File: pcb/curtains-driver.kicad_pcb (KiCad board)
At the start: 2 copper layers, 71 x 29.7 mm, 25 parts, among them J1 Barrel_Jack, J2 UART, J3 Motor, SW1 Reed_NC, SW2 Reed_NC, SW3 UP, SW4 DOWN, SW5 FLASH, U1 ESP-12F, U2 LM1117-3.3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

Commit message: Refactor Circuit
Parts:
- removed R9: 10K, Resistor_SMD:R_0805_2012Metric_Pad1.15x1.40mm_HandSolder
- added C5: 0.1uF, Capacitor_SMD:C_1206_3216Metric_Pad1.42x1.75mm_HandSolder, B.Cu at (115.8, 90.2)
- added SW6: RESET, Button_Switch_SMD:SW_SPST_CK_RS282G05A3, F.Cu at (110.7, 76.3)
- R1, R2, R3, R4: value 10K -> R; moved to B.Cu
- R5, R6, R7: value 10K -> R
- R8: value 5K1 -> 56K
- SW5: footprint Connector_PinHeader_2.54mm:PinHeader_1x02_P2.54mm_Vertical -> Button_Switch_SMD:SW_SPST_CK_RS282G05A3
- moved J1 44.7 mm to (90.7, 83.3), turned to 90 degrees
- moved C4 35.3 mm to (91.5, 76.2), turned to 180 degrees
- moved C2 30.7 mm to (98.8, 74.9), turned to 0 degrees
- moved U2 30.1 mm to (94.1, 69.0)
- moved J2 26.4 mm to (80.8, 65.5), turned to 90 degrees
- moved SW4 19.7 mm to (128.1, 70.2), turned to 90 degrees
- moved SW1 17.3 mm to (128.1, 83.0), turned to 90 degrees
- moved SW3 14.2 mm to (128.1, 76.0), turned to 90 degrees
- moved R4 13.2 mm to (118.5, 85.4), turned to 270 degrees
- moved SW5 12.8 mm to (105.4, 76.3), turned to 270 degrees
- moved R1 10.6 mm to (119.5, 72.4), turned to 0 degrees
- moved SW2 9.40 mm to (128.1, 88.8), turned to 90 degrees
- moved R2 8.70 mm to (119.5, 76.4), turned to 0 degrees
- moved R7 6.52 mm to (96.8, 80.4), turned to 0 degrees
- moved R8 5.86 mm to (119.5, 70.4), turned to 0 degrees
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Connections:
- C4 pad 1: +3V3 -> VCC
- J2 pad 4: +3V3 -> VCC
- R1 pad 1: +3V3 -> Net-(R1-Pad1)
- R1 pad 2: Net-(C1-Pad1) -> VCC
- R2 pad 1: +3V3 -> Net-(R2-Pad1)
- R2 pad 2: Net-(C3-Pad1) -> VCC
- R3 pad 1: +3V3 -> Net-(C1-Pad1)
- R3 pad 2: Net-(R3-Pad2) -> VCC
- R4 pad 1: +3V3 -> Net-(C3-Pad1)
- R4 pad 2: Net-(R4-Pad2) -> VCC
- R5 pad 1: +3V3 -> Earth
- R6 pad 1: +3V3 -> VCC
- R7 pad 1: Earth -> VCC
- SW3 pad 1: +3V3 -> VCC
- SW3 pad 2: Net-(R8-Pad2) -> ADC
- SW4 pad 1: +3V3 -> VCC
- SW4 pad 2: Net-(R9-Pad2) -> Net-(R8-Pad2)
- SW5 pad 1: Earth -> Net-(R7-Pad2)
- SW5 pad 2: Net-(R5-Pad2) -> Earth
- U1 pad 1: Net-(R4-Pad2) -> Net-(R1-Pad1)
- U1 pad 10: Net-(R7-Pad2) -> Net-(R5-Pad2)
- U1 pad 12: Net-(R5-Pad2) -> Net-(R7-Pad2)
- U1 pad 3: Net-(R3-Pad2) -> Net-(R2-Pad1)
- U1 pad 8: +3V3 -> VCC
- U2 pad 2: +3V3 -> VCC
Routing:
- net VCC: track 0.00 -> 132.2 mm, vias 0 -> 2
- net +3V3: track 114.7 -> 0.00 mm
- net +5V: track 115.8 -> 30.8 mm, vias 0 -> 1
- net Net-(C1-Pad1): track 40.6 -> 13.8 mm, vias 1 -> 0
- net Net-(R9-Pad2): track 19.0 -> 0.00 mm, vias 1 -> 0
- net ADC: track 11.4 -> 29.6 mm
- net Net-(C3-Pad1): track 32.1 -> 15.7 mm, vias 1 -> 0
- net Net-(R7-Pad2): track 4.13 -> 15.2 mm, vias 0 -> 1
- net Net-(R5-Pad2): track 11.2 -> 3.26 mm
- net Net-(R1-Pad1): track 0.00 -> 7.76 mm, vias 0 -> 1
- net Net-(R8-Pad2): track 15.0 -> 8.65 mm, vias 1 -> 0
- net Net-(R6-Pad2): track 7.39 -> 3.26 mm
- net Net-(R3-Pad2): track 4.11 -> 0.00 mm, vias 1 -> 0
- net Net-(R4-Pad2): track 4.05 -> 0.00 mm, vias 1 -> 0
- net Net-(R2-Pad1): track 0.00 -> 3.42 mm
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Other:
- board size 71 x 29.7 mm -> 55 x 29.7 mm
- net class Resistor Array added: clearance 0.3, trace_width 0.6, via_dia 0.8, via_drill 0.4
- board text added: "brnv.ru"
- board text added: "curtains driver v1.1"

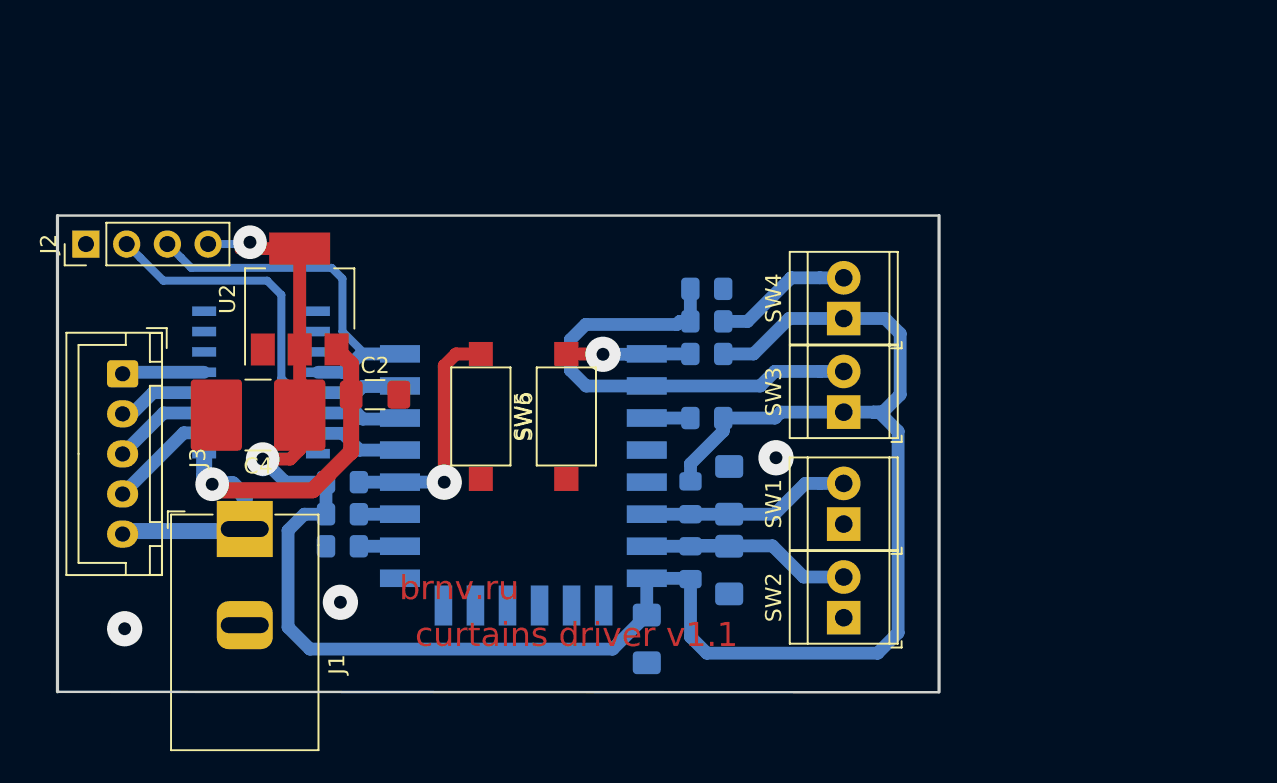
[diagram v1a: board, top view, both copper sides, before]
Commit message: Add USB-UART chip
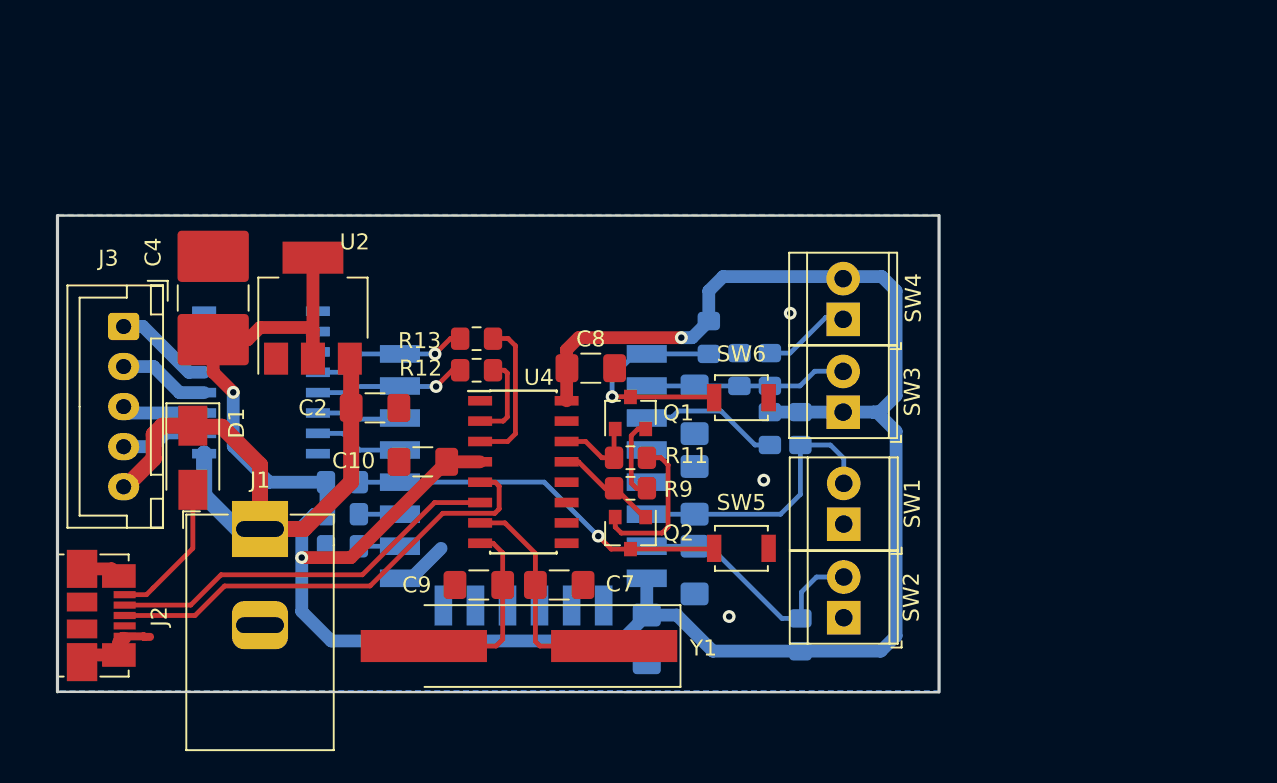
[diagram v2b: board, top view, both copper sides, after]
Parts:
- added C10: 10uF, Capacitor_SMD:C_1206_3216Metric_Pad1.42x1.75mm_HandSolder, F.Cu at (101.8, 79.1)
- added C6: 0.1uF, Capacitor_SMD:C_1206_3216Metric_Pad1.42x1.75mm_HandSolder, B.Cu at (118.7, 75.9)
- added C7: 22pF, Capacitor_SMD:C_1206_3216Metric_Pad1.42x1.75mm_HandSolder, F.Cu at (110.3, 86.8)
- added C8: 10uF, Capacitor_SMD:C_1206_3216Metric_Pad1.42x1.75mm_HandSolder, F.Cu at (112.3, 73.3)
- added C9: 22pF, Capacitor_SMD:C_1206_3216Metric_Pad1.42x1.75mm_HandSolder, F.Cu at (105.3, 86.8)
- added D1: M7, Diode_SMD:D_SMA, F.Cu at (87.4, 78.9)
- added Q1: S8050, Package_TO_SOT_SMD:SOT-23, F.Cu at (114.7, 76.1)
- added Q2: S8050, Package_TO_SOT_SMD:SOT-23, F.Cu at (114.7, 83.6)
- added R11: 10K, Resistor_SMD:R_0805_2012Metric_Pad1.15x1.40mm_HandSolder, F.Cu at (114.7, 78.9)
- added R12: 470, Resistor_SMD:R_0805_2012Metric_Pad1.15x1.40mm_HandSolder, F.Cu at (105.1, 73.4)
- added R13: 470, Resistor_SMD:R_0805_2012Metric_Pad1.15x1.40mm_HandSolder, F.Cu at (105.1, 71.4)
- added R9: 10K, Resistor_SMD:R_0805_2012Metric_Pad1.15x1.40mm_HandSolder, F.Cu at (114.7, 80.8)
- added U4: CH340G, Package_SO:SOIC-16_3.9x9.9mm_P1.27mm, F.Cu at (108.1, 79.8)
- added Y1: HC-49, Crystal:Crystal_SMD_HC49-SD_HandSoldering, F.Cu at (107.8, 90.6)
- J2: value UART -> USB_B_Micro; footprint Connector_PinHeader_2.54mm:PinHeader_1x04_P2.54mm_Vertical -> Connector_USB:USB_Micro-B_Molex_47346-0001
- R1, R2, R3, R4, R5, R6, R7: value R -> 10K
- SW5, SW6: footprint Button_Switch_SMD:SW_SPST_CK_RS282G05A3 -> Button_Switch_SMD:SW_SPST_B3U-1000P
- moved J2 23.2 mm to (81.7, 88.7), turned to 270 degrees
- moved SW5 18.2 mm to (121.7, 84.5), turned to 0 degrees
- moved SW6 11.0 mm to (121.7, 75.1), turned to 180 degrees
- moved R4 8.20 mm to (125.3, 89.9)
- moved R3 8.10 mm to (125.3, 77.0)
- moved C4 7.82 mm to (88.7, 68.9), turned to 90 degrees
- moved R10 5.43 mm to (121.5, 73.4), turned to 270 degrees
- moved R8 4.95 mm to (123.4, 73.4), turned to 90 degrees
- moved R2 3.99 mm to (123.4, 77.0), turned to 90 degrees
- moved J3 2.95 mm to (83.1, 70.7)
- moved C1 2.16 mm to (118.7, 80.9)
- moved C3 2.16 mm to (118.7, 85.9)
- moved R1 1.04 mm to (119.6, 71.4), turned to 90 degrees
- moved U2 1.00 mm to (94.9, 69.5)
- moved J1 0.95 mm to (91.6, 83.3)
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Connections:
- net Net-(R1-Pad1) renamed RST
- net Net-(R7-Pad2) renamed GPIO0
- J2 pad 1: Earth -> Net-(D1-Pad2)
- J2 pad 4: VCC -> Net-(J2-Pad4)
- SW4 pad 1: VCC -> Net-(R8-Pad2)
- SW4 pad 2: Net-(R8-Pad2) -> VCC
- U1 pad 15: Net-(J2-Pad2) -> RXD
- U1 pad 16: Net-(J2-Pad3) -> TXD
- U3 pad 4: Net-(J2-Pad3) -> TXD
- U3 pad 5: Net-(J2-Pad2) -> RXD
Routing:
- net Net-(C7-Pad1): track 0.00 -> 19.2 mm
- net VCC: track 132.2 -> 150.4 mm, vias 2 -> 3
- net ADC: track 29.6 -> 13.3 mm
- net Net-(C9-Pad1): track 0.00 -> 11.9 mm
- net Earth: track 0.00 -> 10.5 mm
- net TXD: track 0.00 -> 9.74 mm, vias 0 -> 1
- net Net-(Q2-Pad2): track 0.00 -> 9.62 mm
- net Net-(R13-Pad2): track 0.00 -> 9.49 mm
- net RXD: track 0.00 -> 9.39 mm, vias 0 -> 1
- net Net-(D1-Pad2): track 0.00 -> 9.10 mm
- net GPIO0: track 15.2 -> 23.9 mm
- net +5V: track 30.8 -> 38.1 mm, vias 1 -> 0
- net RST: track 7.76 -> 14.3 mm
- net Net-(Q2-Pad1): track 0.00 -> 6.36 mm
- net Net-(R2-Pad1): track 3.42 -> 9.32 mm
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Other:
- net class Default: clearance 0.3 -> 0.15; trace_width 0.8 -> 0.3
- rule trace_clearance: 0.3 -> 0.15
- board text removed: "brnv.ru"
- board text removed: "curtains driver v1.1"

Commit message: Update PCB
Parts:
- added R14: 10K, Resistor_SMD:R_0805_2012Metric_Pad1.15x1.40mm_HandSolder, B.Cu at (97.4, 72.5)
- U3: value ULN2003 -> ULN2003A
- Y1: footprint Crystal:Crystal_SMD_HC49-SD_HandSoldering -> Crystal:Crystal_SMD_SeikoEpson_FA238V-4Pin_3.2x2.5mm_HandSoldering
- flash: renamed from SW5; footprint Button_Switch_SMD:SW_SPST_B3U-1000P -> Button_Switch_SMD:SW_SPST_TL3342
- reed 1: renamed from SW2
- reed 2: renamed from SW1
- reset: renamed from SW6; footprint Button_Switch_SMD:SW_SPST_B3U-1000P -> Button_Switch_SMD:SW_SPST_TL3342
- moved flash 3.46 mm to (120.7, 87.8), turned to 90 degrees
- moved reset 2.70 mm to (120.7, 77.6), turned to 270 degrees
- moved C7 2.60 mm to (112.3, 88.5), turned to 270 degrees
- moved C9 2.45 mm to (103.5, 88.5), turned to 270 degrees
- moved Y1 2.15 mm to (107.9, 88.5)
- moved reed 1 1.12 mm to (128.0, 90.0)
- moved D1 0.97 mm to (87.8, 78.0)
- moved C5 0.79 mm to (115.8, 91.0)
- moved UP 0.52 mm to (128.0, 76.5)
- moved R2 0.52 mm to (123.4, 77.6)
- moved R3 0.52 mm to (125.3, 77.6)
- moved DOWN 0.41 mm to (128.0, 69.8)
- moved R5 0.28 mm to (96.8, 84.7)
- moved R6 0.28 mm to (96.8, 82.7)
- moved R7 0.28 mm to (96.8, 80.7)
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- renumbered SW4 to DOWN, SW3 to UP
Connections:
- DOWN pad 1: Net-(R8-Pad2) -> VCC
- DOWN pad 2: VCC -> Net-(R8-Pad2)
- Y1 pad 2: Net-(C9-Pad1) -> Net-(Y1-Pad2)
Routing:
- net Net-(C7-Pad1): track 19.2 -> 12.1 mm
- net RST: track 14.3 -> 20.1 mm
- net GPIO0: track 23.9 -> 29.2 mm
- net Net-(C9-Pad1): track 11.9 -> 8.77 mm
- net Net-(R8-Pad2): track 5.50 -> 8.17 mm, vias 0 -> 1
- net VCC: track 150.4 -> 153.0 mm, vias 3 -> 4
- net Net-(D1-Pad2): track 9.10 -> 11.6 mm
- net Net-(C3-Pad1): track 17.0 -> 16.1 mm
- net Net-(C1-Pad1): track 18.6 -> 17.8 mm
- net +5V: track 38.1 -> 38.7 mm
- net Earth: vias 3 -> 8

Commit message: Minimal working result
Signed-off-by: Mikhail Baranov <mikhail.baranov@gmail.com>
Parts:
- removed reed 2: Reed_NC, TerminalBlock_TE-Connectivity:TerminalBlock_TE_282834-2_1x02_P2.54mm_Horizontal
- added J4: Conn_01x02_Male, Connector_PinHeader_2.54mm:PinHeader_1x02_P2.54mm_Horizontal, F.Cu at (140.5, 82.8)
- added J5: Conn_01x02_Male, Connector_PinHeader_2.54mm:PinHeader_1x02_P2.54mm_Horizontal, F.Cu at (149.7, 82.9)
- added J6: Reed_1, TerminalBlock_TE-Connectivity:TerminalBlock_TE_282834-2_1x02_P2.54mm_Horizontal, F.Cu at (128.0, 80.8)
- added J7: Reed_1, TerminalBlock_TE-Connectivity:TerminalBlock_TE_282834-2_1x02_P2.54mm_Horizontal, F.Cu at (128.0, 87.4)
- added SW1: Reed_NC, symbols:Reed_Switch_L20mm_W3mm_P26mm, F.Cu at (139.2, 66.5)
- SW2: renamed from reed 1; footprint TerminalBlock_TE-Connectivity:TerminalBlock_TE_282834-2_1x02_P2.54mm_Horizontal -> symbols:Reed_Switch_L20mm_W3mm_P26mm
- moved SW2 31.0 mm to (148.5, 66.6)
- renumbered UP to SW3, DOWN to SW4, flash to SW5, reset to SW6
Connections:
- SW2 pad 1: Earth -> /reed_out_2
- SW2 pad 2: Net-(C3-Pad1) -> /reed_in_2
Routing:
- net /reed_in_1: track 0.00 -> 29.6 mm
- net /reed_in_2: track 0.00 -> 29.3 mm
- net /reed_out_2: track 0.00 -> 4.78 mm
- net /reed_out_1: track 0.00 -> 4.71 mm
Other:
- board size 55 x 29.7 mm -> 73 x 41.4 mm

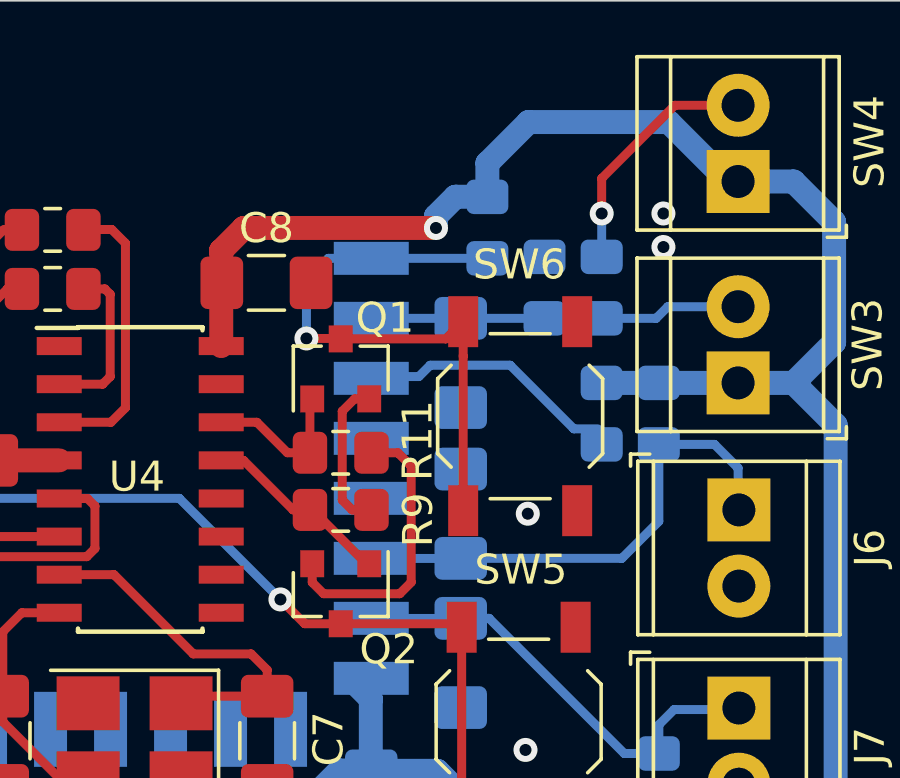
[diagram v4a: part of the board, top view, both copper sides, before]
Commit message: Change PWM and UART circuit
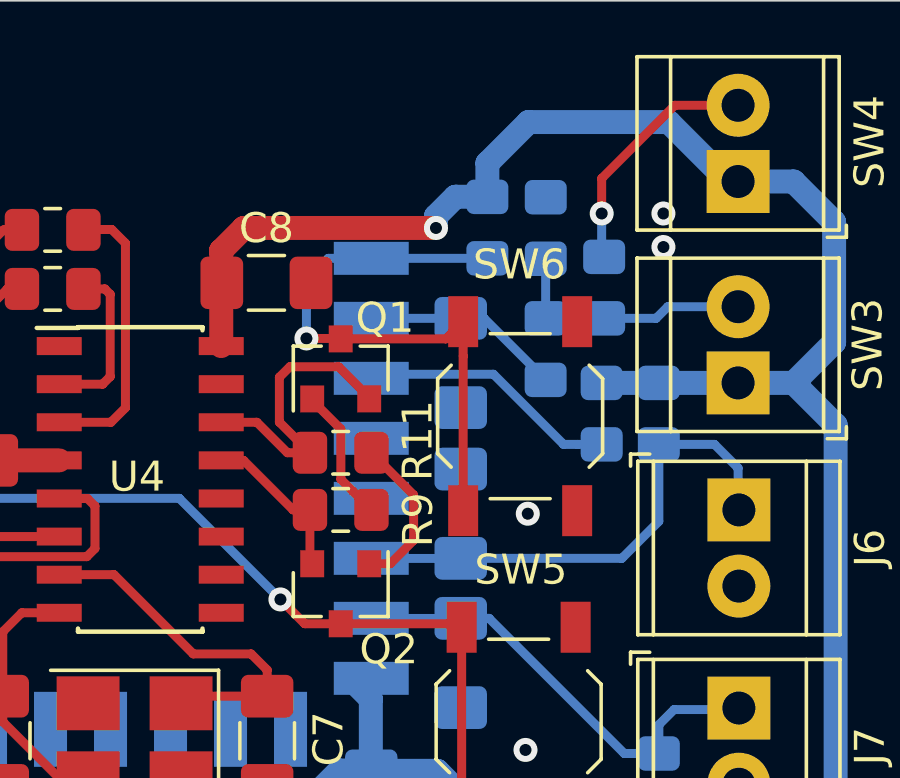
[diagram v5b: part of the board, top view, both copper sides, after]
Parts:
- added R15: 1K, Resistor_SMD:R_0805_2012Metric_Pad1.15x1.40mm_HandSolder, B.Cu at (121.6, 75.4)
- C6: value 0.1uF -> 10nF
- R8: value 56K -> 10K
- moved R10 1.99 mm to (121.6, 71.4)
- moved R8 0.08 mm to (123.5, 73.4)
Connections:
- net Net-(J2-Pad2) renamed /D-
- net Net-(J2-Pad3) renamed /D+
- R10 pad 2: ADC -> Net-(R10-Pad2)
- R11 pad 1: Net-(Q2-Pad2) -> Net-(Q2-Pad1)
- R11 pad 2: Net-(Q1-Pad1) -> Net-(Q1-Pad2)
- R8 pad 1: ADC -> Net-(R10-Pad2)
- R9 pad 1: Net-(Q1-Pad2) -> Net-(Q1-Pad1)
- R9 pad 2: Net-(Q2-Pad1) -> Net-(Q2-Pad2)
- SW3 pad 2: ADC -> Net-(R10-Pad2)
- U4 pad 13: Net-(Q2-Pad1) -> Net-(Q2-Pad2)
- U4 pad 14: Net-(Q1-Pad1) -> Net-(Q1-Pad2)
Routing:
- net Net-(R10-Pad2): track 0.00 -> 8.65 mm
- net ADC: track 13.1 -> 7.36 mm
- net Net-(Q1-Pad2): track 5.14 -> 10.1 mm
- net Net-(Q2-Pad2): track 9.62 -> 5.55 mm
- net Net-(Q2-Pad1): track 6.36 -> 5.40 mm
- net Net-(Q1-Pad1): track 5.20 -> 4.62 mm

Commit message: Make terminals labels visible after wirig
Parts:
- R10: value 10K -> 2K2
- moved SW3 1.30 mm to (129.3, 76.5)
- moved SW4 1.30 mm to (129.3, 69.8)
- moved J6 1.27 mm to (129.3, 80.8)
- moved J7 1.27 mm to (129.3, 87.4)
- moved R3 0.38 mm to (125.7, 77.6)
- moved R2 0.25 mm to (123.7, 77.6)
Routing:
- net VCC: track 153.0 -> 155.3 mm
- net Net-(R8-Pad2): track 8.17 -> 9.47 mm
- net Net-(R10-Pad2): track 8.65 -> 9.85 mm
- net Net-(C1-Pad1): track 17.8 -> 18.9 mm
- net Net-(C3-Pad1): track 16.1 -> 16.8 mm
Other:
- board text added: "DOWN"
- board text added: "REED 1"
- board text added: "REED 2"
- board text added: "UP"

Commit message: Update PCB
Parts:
- removed J4, J5: Conn_01x02_Male, Connector_PinHeader_2.54mm:PinHeader_1x02_P2.54mm_Horizontal
- removed SW1, SW2: Reed_NC, symbols:Reed_Switch_L20mm_W3mm_P26mm
- moved D1 2.06 mm to (89.6, 79.0), turned to 180 degrees
- moved R5 1.97 mm to (97.8, 86.4), turned to 90 degrees
- moved U3 1.53 mm to (90.4, 75.0)
- moved R14 1.24 mm to (97.0, 71.4)
- moved R6 0.76 mm to (96.8, 83.4)
- moved R7 0.76 mm to (96.8, 81.4)
- renumbered SW5 to FLASH, SW6 to RESET
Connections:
- U3 pad 4: TXD -> RXD
- U3 pad 5: RXD -> Net-(U1-Pad14)
- U3 pad 6: Net-(U1-Pad14) -> Net-(U1-Pad13)
- U3 pad 7: Net-(U1-Pad13) -> Net-(R6-Pad2)
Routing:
- net /reed_in_1: track 29.6 -> 0.00 mm
- net /reed_in_2: track 29.3 -> 0.00 mm
- net Net-(R6-Pad2): track 3.39 -> 11.7 mm
- net /reed_out_2: track 4.78 -> 0.00 mm
- net /reed_out_1: track 4.71 -> 0.00 mm
- net TXD: track 9.74 -> 7.51 mm
- net VCC: track 155.3 -> 153.7 mm
- net Net-(U1-Pad14): track 6.00 -> 7.48 mm
- net Net-(U1-Pad13): track 6.25 -> 7.69 mm
- net RXD: track 9.39 -> 10.5 mm
- net Net-(J3-Pad4): track 4.84 -> 3.76 mm
- net Net-(J3-Pad3): track 5.19 -> 4.27 mm
- net Net-(D1-Pad2): track 11.6 -> 12.5 mm
- net Net-(J3-Pad2): track 5.70 -> 4.80 mm
- net +5V: track 38.7 -> 37.8 mm
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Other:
- board size 73 x 41.4 mm -> 55 x 29.7 mm
- board text added: "Curtain Driver v2 brnv.ru"
- board text added: "JLCJLCJLCJLC"
